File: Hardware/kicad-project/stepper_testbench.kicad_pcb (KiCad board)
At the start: 2 copper layers, 74.3 x 120.1 mm, 9 parts, among them CN11 Conn_02x35_Odd_Even, CN12 Conn_02x35_Odd_Even, J1 Conn_01x08_Male, U1 LM358P, U2 LEM-CAS-6NP, U3 LM358P, U4 LM358P, U5 LM317_TO-263

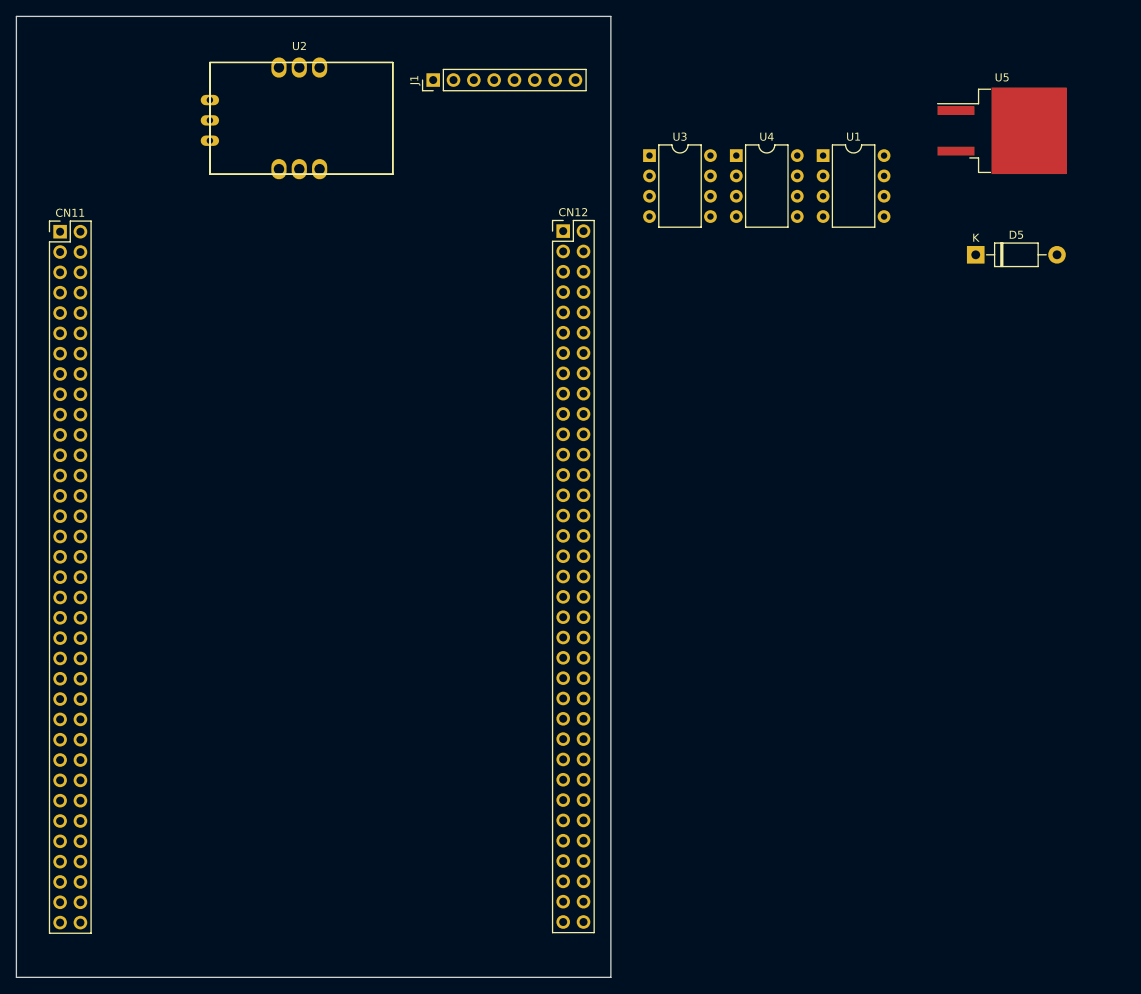
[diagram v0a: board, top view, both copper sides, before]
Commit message: fw: add led state pin to ioc
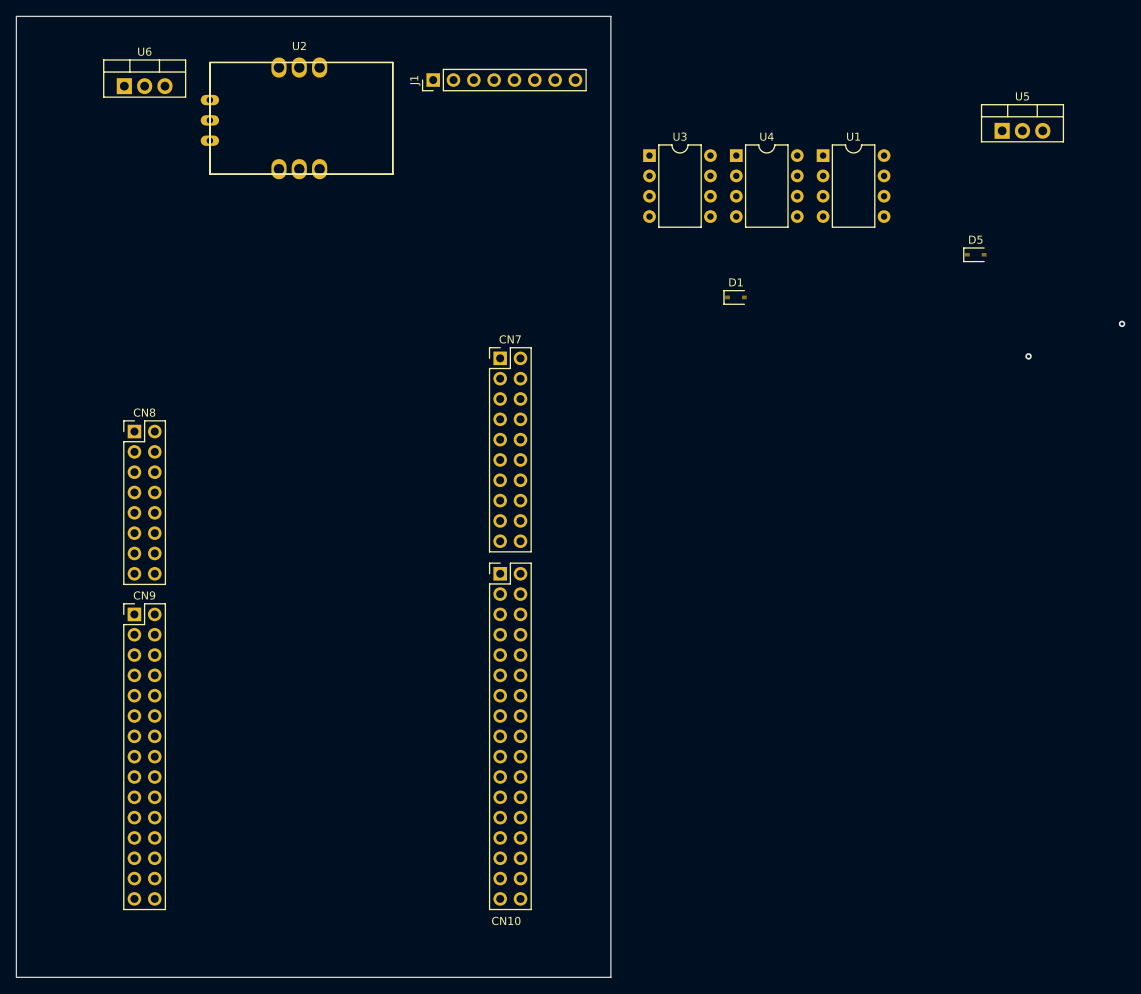
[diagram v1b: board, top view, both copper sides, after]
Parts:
- removed CN11, CN12: Conn_02x35_Odd_Even, Connector_PinHeader_2.54mm:PinHeader_2x35_P2.54mm_Vertical
- added CN10: Conn_02x17_Odd_Even, Connector_PinHeader_2.54mm:PinHeader_2x17_P2.54mm_Vertical, F.Cu at (165.9, 95.8)
- added CN7: Conn_02x10_Odd_Even, Connector_PinHeader_2.54mm:PinHeader_2x10_P2.54mm_Vertical, F.Cu at (165.9, 68.8)
- added CN8: Conn_02x08_Odd_Even, Connector_PinHeader_2.54mm:PinHeader_2x08_P2.54mm_Vertical, F.Cu at (120.1, 78.0)
- added CN9: Conn_02x15_Odd_Even, Connector_PinHeader_2.54mm:PinHeader_2x15_P2.54mm_Vertical, F.Cu at (120.1, 100.8)
- added D1: DIODE, Diode_SMD:D_SOD-323, F.Cu at (195.3, 61.2)
- added U6: L7805, Package_TO_SOT_THT:TO-220-3_Vertical, F.Cu at (118.9, 34.8)
- D5: footprint Diode_THT:D_DO-41_SOD81_P10.16mm_Horizontal -> Diode_SMD:D_SOD-323
- U5: footprint Package_TO_SOT_SMD:TO-263-2 -> Package_TO_SOT_THT:TO-220-3_Vertical
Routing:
- net GND: vias 0 -> 2
